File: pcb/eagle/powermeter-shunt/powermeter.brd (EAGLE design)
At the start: 99.6 x 74.6 mm, 29 parts, among them IC1 INA126P, IC2 LM324N, IC3 MCP3208, IC4 MEA1D0512SC

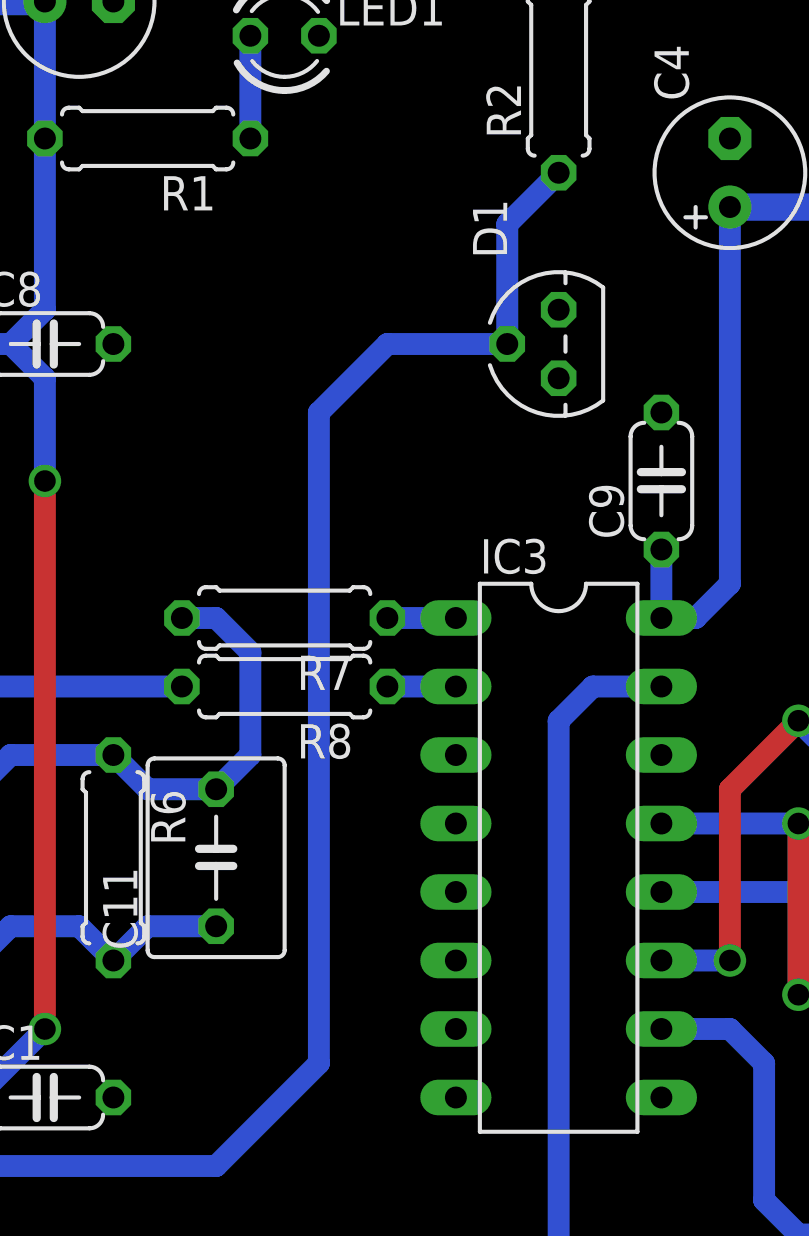
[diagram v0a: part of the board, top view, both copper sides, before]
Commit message: Made design compatible with MCP3204 (can now use MCP3204 or MCP3208)
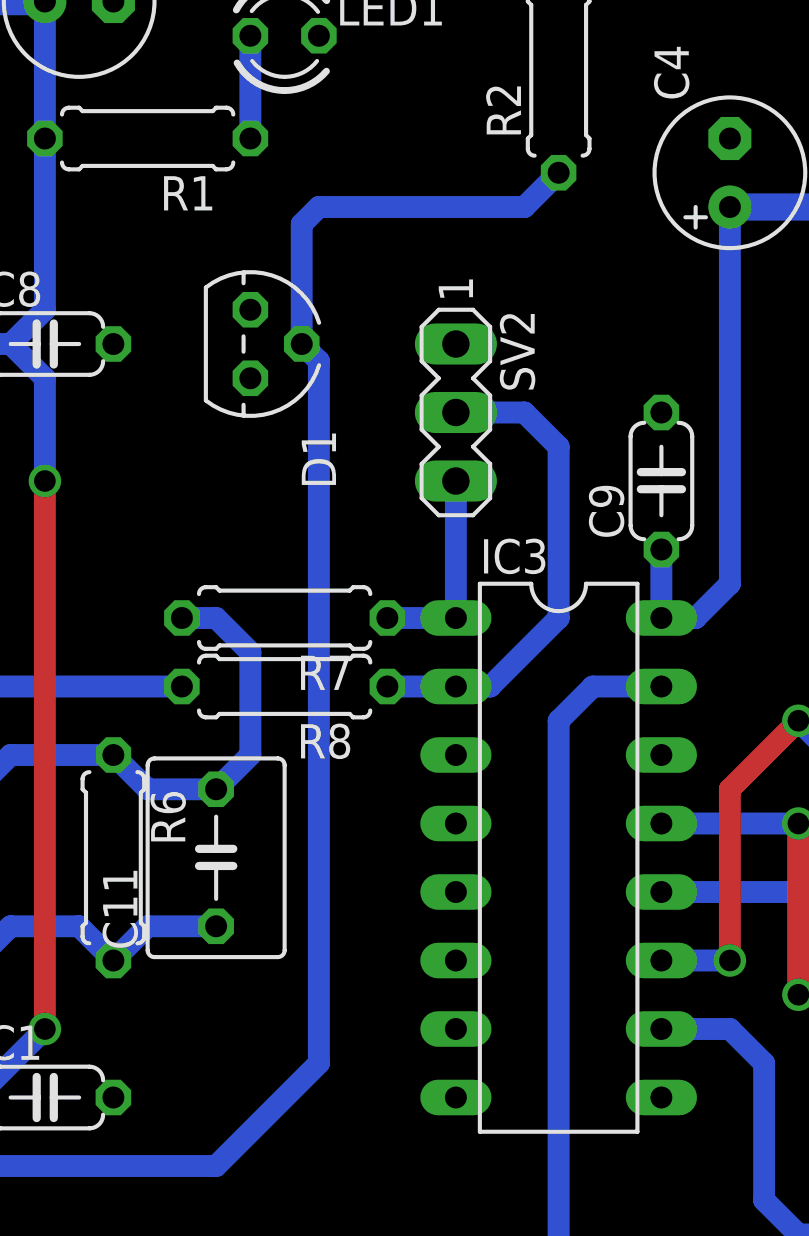
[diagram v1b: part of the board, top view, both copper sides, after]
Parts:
- added SV2: (no value), con-lstb:MA03-1
- moved D1 11.4 mm to (57.1, 41.9), turned to 270 degrees
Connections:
- removed net N$10: IC3.CH0, R7.1
- removed net VSAMPLE: IC3.CH1, R8.1
- new net VM1: IC3.CH1, R8.1, SV2.2
- new net VM2: IC3.CH0, R7.1, SV2.3
- net GND: now also IC3.CH6, SV2.1
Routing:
- net VM1: track 0.00 -> 18.1 mm
- net VM2: track 0.00 -> 7.62 mm
- net VSAMPLE: track 2.54 -> 0.00 mm
- net N$10: track 2.54 -> 0.00 mm
- net N$14: track 56.1 -> 58.5 mm
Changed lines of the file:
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@@
 <hole x="95.25" y="3.81" drill="3.2"/>
 <hole x="95.25" y="71.12" drill="3.2"/>
+<circle x="3.81" y="71.12" radius="3.5" width="0" layer="42"/>
+<circle x="95.25" y="71.12" radius="3.5" width="0" layer="42"/>
+<circle x="95.25" y="3.81" radius="3.5" width="0" layer="42"/>
+<circle x="3.81" y="3.81" radius="3.5" width="0" layer="42"/>
 </plain>
 <attributes>
@@
 <attribute name="OC_FARNELL" value="unknown" x="12.7" y="34.29" size="1.778" layer="27" rot="R90" display="off"/>
 </element>
-<element name="D1" library="lm385" package="TO-92" value="LM385" x="68.58" y="41.91" rot="R90"/>
+<element name="D1" library="lm385" package="TO-92" value="LM385" x="57.15" y="41.91" rot="R270"/>
 <element name="IC2" library="linear" package="DIL14" value="LM324N" x="40.64" y="13.97" rot="R90"/>
 <element name="R2" library="rcl" package="0207/7" value="4.7k" x="68.58" y="52.07" rot="R90"/>
@@
 <element name="LED1" library="led" package="LED3MM" value="" x="58.42" y="53.34"/>
 <element name="R1" library="rcl" package="0207/7" value="1k" x="53.34" y="49.53" rot="R180"/>
+<element name="SV2" library="con-lstb" package="MA03-1" value="" x="64.77" y="39.37" rot="R270">
+<attribute name="OC_NEWARK" value="unknown" x="64.77" y="39.37" size="1.778" layer="27" rot="R270" display="off"/>
+<attribute name="MPN" value="" x="64.77" y="39.37" size="1.778" layer="27" rot="R270" display="off"/>
+<attribute name="MF" value="" x="64.77" y="39.37" size="1.778" layer="27" rot="R270" display="off"/>
+<attribute name="OC_FARNELL" value="unknown" x="64.77" y="39.37" size="1.778" layer="27" rot="R270" display="off"/>
+</element>
 </elements>
 <signals>
@@
 </polygon>
 <contactref element="LED1" pad="K"/>
+<contactref element="SV2" pad="1"/>
+<contactref element="IC3" pad="CH6"/>
 </signal>
 <signal name="+5V">
@@
 <wire x1="45.72" y1="39.37" x2="44.45" y2="39.37" width="0.8128" layer="16"/>
 </signal>
-<signal name="N$10">
+<signal name="VM2">
 <contactref element="R7" pad="1"/>
 <contactref element="IC3" pad="CH0"/>
 <wire x1="62.23" y1="31.75" x2="64.77" y2="31.75" width="0.8128" layer="16"/>
-</signal>
-<signal name="VSAMPLE">
+<contactref element="SV2" pad="3"/>
+<wire x1="64.77" y1="31.75" x2="64.77" y2="36.83" width="0.8128" layer="16"/>
+</signal>
+<signal name="VM1">
 <contactref element="IC3" pad="CH1"/>
 <contactref element="R8" pad="1"/>
 <wire x1="62.23" y1="29.21" x2="64.77" y2="29.21" width="0.8128" layer="16"/>
+<contactref element="SV2" pad="2"/>
+<wire x1="64.77" y1="29.21" x2="66.04" y2="29.21" width="0.8128" layer="16"/>
+<wire x1="66.04" y1="29.21" x2="68.58" y2="31.75" width="0.8128" layer="16"/>
+<wire x1="68.58" y1="31.75" x2="68.58" y2="38.1" width="0.8128" layer="16"/>
+<wire x1="68.58" y1="38.1" x2="67.31" y2="39.37" width="0.8128" layer="16"/>
+<wire x1="67.31" y1="39.37" x2="64.77" y2="39.37" width="0.8128" layer="16"/>
 </signal>
 <signal name="N$9">
@@
 <wire x1="55.88" y1="11.43" x2="59.69" y2="15.24" width="0.8128" layer="16"/>
 <wire x1="55.88" y1="11.43" x2="44.45" y2="11.43" width="0.8128" layer="16"/>
-<wire x1="66.675" y1="41.91" x2="66.675" y2="46.355" width="0.8128" layer="16"/>
-<wire x1="66.675" y1="46.355" x2="68.58" y2="48.26" width="0.8128" layer="16"/>
-<wire x1="66.675" y1="41.91" x2="62.23" y2="41.91" width="0.8128" layer="16"/>
-<wire x1="62.23" y1="41.91" x2="59.69" y2="39.37" width="0.8128" layer="16"/>
-<wire x1="59.69" y1="39.37" x2="59.69" y2="15.24" width="0.8128" layer="16"/>
+<wire x1="59.69" y1="41.275" x2="59.69" y2="15.24" width="0.8128" layer="16"/>
+<wire x1="59.69" y1="41.275" x2="59.055" y2="41.91" width="0.8128" layer="16"/>
+<wire x1="59.055" y1="41.91" x2="59.055" y2="46.355" width="0.8128" layer="16"/>
+<wire x1="59.055" y1="46.355" x2="59.69" y2="46.99" width="0.8128" layer="16"/>
+<wire x1="59.69" y1="46.99" x2="67.31" y2="46.99" width="0.8128" layer="16"/>
+<wire x1="67.31" y1="46.99" x2="68.58" y2="48.26" width="0.8128" layer="16"/>
 </signal>
 </signals>
